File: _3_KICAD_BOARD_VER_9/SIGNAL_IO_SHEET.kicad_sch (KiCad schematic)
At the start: 5 parts, among them U3 DAC7564ICPW

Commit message: feat : dim board base board 작업시작
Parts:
- C18, C19, C20: LCSC Part # (none) -> C14663
- R1: LCSC Part # (none) -> C105588
- U3: LCSC Part # (none) -> C52451
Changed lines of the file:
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@@
+			)
+		)
+		(property "LCSC Part #" "C14663"
+			(at 139.7 58.42 0)
+			(effects
+				(font
+					(size 1.27 1.27)
+				)
+				(hide yes)
 			)
 		)
@@
 			)
 		)
+		(property "LCSC Part #" "C105588"
+			(at 63.5 93.98 90)
+			(effects
+				(font
+					(size 1.27 1.27)
+				)
+				(hide yes)
+			)
+		)
 		(pin "1"
 		)
@@
 			)
 		)
+		(property "LCSC Part #" "C52451"
+			(at 106.68 81.28 0)
+			(effects
+				(font
+					(size 1.27 1.27)
+				)
+				(hide yes)
+			)
+		)
 		(pin "15"
 		)
@@
 			)
 		)
+		(property "LCSC Part #" "C14663"
+			(at 72.39 96.52 0)
+			(effects
+				(font
+					(size 1.27 1.27)
+				)
+				(hide yes)
+			)
+		)
 		(pin "1"
 		)
@@
 			(at 151.13 53.34 0)
 			(effects
+				(font
+					(size 1.27 1.27)
+				)
+				(hide yes)
+			)
+		)
+		(property "LCSC Part #" "C14663"
+			(at 151.13 53.34 0)
+			(effects

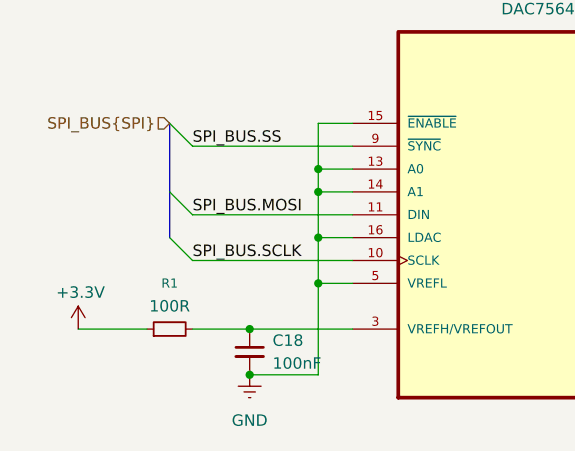
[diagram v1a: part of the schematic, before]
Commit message: feat : 회로도 수정, MCLR pull up 10K 추가, GND MCU쪽 floating 다수...
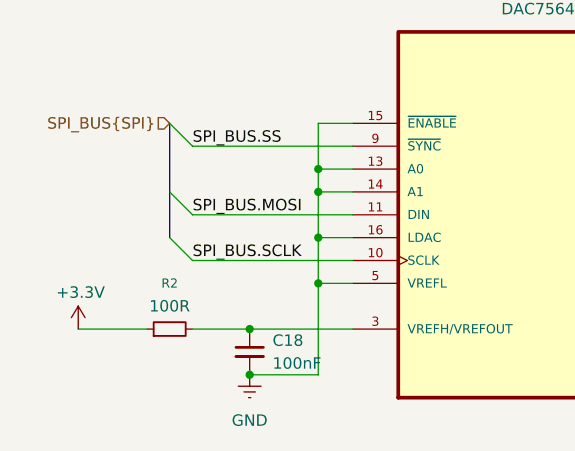
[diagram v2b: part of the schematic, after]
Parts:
- renumbered R1 to R2
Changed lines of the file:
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@@
 		(dnp no)
 		(fields_autoplaced yes)
-		(property "Reference" "#PWR024"
+		(property "Reference" "#PWR025"
 			(at 129.54 105.41 0)
 			(effects
@@
 			(project "_3_KICAD_BOARD_VER_9"
 				(path "/04989ac4-daca-49e5-abaa-7cb085fca6f2/1ca575b3-52ba-4d80-bf98-4be170f12692"
-					(reference "#PWR024")
+					(reference "#PWR025")
 					(unit 1)
 				)
@@
 		(dnp no)
 		(fields_autoplaced yes)
-		(property "Reference" "#PWR028"
+		(property "Reference" "#PWR029"
 			(at 151.13 62.23 0)
 			(effects
@@
 			(project "_3_KICAD_BOARD_VER_9"
 				(path "/04989ac4-daca-49e5-abaa-7cb085fca6f2/1ca575b3-52ba-4d80-bf98-4be170f12692"
-					(reference "#PWR028")
+					(reference "#PWR029")
 					(unit 1)
 				)
@@
 		(on_board yes)
 		(dnp no)
-		(property "Reference" "#PWR027"
+		(property "Reference" "#PWR028"
 			(at 151.13 53.34 0)
 			(effects
@@
 			(project "_3_KICAD_BOARD_VER_9"
 				(path "/04989ac4-daca-49e5-abaa-7cb085fca6f2/1ca575b3-52ba-4d80-bf98-4be170f12692"
-					(reference "#PWR027")
+					(reference "#PWR028")
 					(unit 1)
 				)
@@
 		(on_board yes)
 		(dnp no)
-		(property "Reference" "#PWR025"
+		(property "Reference" "#PWR026"
 			(at 139.7 59.69 0)
 			(effects
@@
 			(project "_3_KICAD_BOARD_VER_9"
 				(path "/04989ac4-daca-49e5-abaa-7cb085fca6f2/1ca575b3-52ba-4d80-bf98-4be170f12692"
-					(reference "#PWR025")
+					(reference "#PWR026")
 					(unit 1)
 				)
@@
 		(dnp no)
 		(fields_autoplaced yes)
-		(property "Reference" "#PWR023"
+		(property "Reference" "#PWR024"
 			(at 72.39 105.41 0)
 			(effects
@@
 			(project "_3_KICAD_BOARD_VER_9"
 				(path "/04989ac4-daca-49e5-abaa-7cb085fca6f2/1ca575b3-52ba-4d80-bf98-4be170f12692"
-					(reference "#PWR023")
+					(reference "#PWR024")
 					(unit 1)
 				)
@@
 		(dnp no)
 		(fields_autoplaced yes)
-		(property "Reference" "R1"
+		(property "Reference" "R2"
 			(at 63.5 88.9 90)
 			(effects
@@
 			(project "_3_KICAD_BOARD_VER_9"
 				(path "/04989ac4-daca-49e5-abaa-7cb085fca6f2/1ca575b3-52ba-4d80-bf98-4be170f12692"
-					(reference "R1")
+					(reference "R2")
 					(unit 1)
 				)
@@
 		(on_board yes)
 		(dnp no)
-		(property "Reference" "#PWR022"
+		(property "Reference" "#PWR023"
 			(at 53.34 97.79 0)
 			(effects
@@
 			(project "_3_KICAD_BOARD_VER_9"
 				(path "/04989ac4-daca-49e5-abaa-7cb085fca6f2/1ca575b3-52ba-4d80-bf98-4be170f12692"
-					(reference "#PWR022")
+					(reference "#PWR023")
 					(unit 1)
 				)
@@
 		(dnp no)
 		(fields_autoplaced yes)
-		(property "Reference" "#PWR026"
+		(property "Reference" "#PWR027"
 			(at 139.7 67.31 0)
 			(effects
@@
 			(project "_3_KICAD_BOARD_VER_9"
 				(path "/04989ac4-daca-49e5-abaa-7cb085fca6f2/1ca575b3-52ba-4d80-bf98-4be170f12692"
-					(reference "#PWR026")
-					(unit 1)
-				)
+					(reference "#PWR027")
+					(unit 1)
+				)
